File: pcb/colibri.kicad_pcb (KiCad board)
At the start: 2 copper layers, 160 x 95.2 mm, 97 parts

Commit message: starting to build the right side
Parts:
- added REF**: Breakaway_Tabs, kbd:Breakaway_Tabs, F.Cu at (75.0, 134.5)
- added REF**: Breakaway_Tabs, kbd:Breakaway_Tabs, F.Cu at (75.0, 230.2)
- added REF**: Breakaway_Tabs, kbd:Breakaway_Tabs, F.Cu at (24.8, 114.2)
- added REF**: Breakaway_Tabs, kbd:Breakaway_Tabs, F.Cu at (75.0, 38.8)
- added REF**: Breakaway_Tabs, kbd:Breakaway_Tabs, F.Cu at (24.8, 210.0)
- added REF**: Breakaway_Tabs, kbd:Breakaway_Tabs, F.Cu at (24.8, 154.8)
- added REF**: Breakaway_Tabs, kbd:Breakaway_Tabs, F.Cu at (24.8, 59.0)
- added REF**: Breakaway_Tabs, kbd:Breakaway_Tabs, F.Cu at (135.0, 134.5)
- added REF**: Breakaway_Tabs, kbd:Breakaway_Tabs, F.Cu at (185.2, 114.2)
- added REF**: Breakaway_Tabs, kbd:Breakaway_Tabs, F.Cu at (185.2, 59.0)
- added REF**: Breakaway_Tabs, kbd:Breakaway_Tabs, F.Cu at (135.0, 38.8)
- added REF**: Breakaway_Tabs, kbd:Breakaway_Tabs, F.Cu at (185.2, 154.8)
- added REF**: Breakaway_Tabs, kbd:Breakaway_Tabs, F.Cu at (185.2, 210.0)
- added REF**: Breakaway_Tabs, kbd:Breakaway_Tabs, F.Cu at (135.0, 230.2)
- added Ref**: Val**, kbd:M2_HOLE_v3, F.Cu at (51.8, 210.9)
- added Ref**: Val**, kbd:M2_HOLE_v3, F.Cu at (51.8, 153.8)
- added Ref**: Val**, kbd:M2_HOLE_v3, F.Cu at (165.0, 210.9)
- added Ref**: Val**, kbd:M2_HOLE_v3, F.Cu at (158.2, 153.8)
- added pro-micro2: ProMicro, kbd:ProMicro_v4, B.Cu at (172.1, 156.1)
- added rd-1: 1N4148W, kbd:D3_SMD_v2, B.Cu at (166.1, 144.3)
- added rd-10: 1N4148W, kbd:D3_SMD_v2, B.Cu at (89.9, 163.3)
- added rd-11: 1N4148W, kbd:D3_SMD_v2, B.Cu at (70.9, 163.3)
- added rd-12: 1N4148W, kbd:D3_SMD_v2, B.Cu at (51.8, 163.3)
- added rd-13: 1N4148W, kbd:D3_SMD_v2, B.Cu at (170.9, 182.4)
- added rd-14: 1N4148W, kbd:D3_SMD_v2, B.Cu at (128.0, 182.4)
- added rd-15: 1N4148W, kbd:D3_SMD_v2, B.Cu at (109.0, 182.4)
- added rd-16: 1N4148W, kbd:D3_SMD_v2, B.Cu at (89.9, 182.4)
- added rd-17: 1N4148W, kbd:D3_SMD_v2, B.Cu at (70.9, 182.4)
- added rd-18: 1N4148W, kbd:D3_SMD_v2, B.Cu at (51.8, 182.4)
- added rd-19: 1N4148W, kbd:D3_SMD_v2, B.Cu at (180.4, 201.4)
- added rd-2: 1N4148W, kbd:D3_SMD_v2, B.Cu at (128.0, 144.3)
- added rd-20: 1N4148W, kbd:D3_SMD_v2, B.Cu at (128.0, 201.4)
- added rd-21: 1N4148W, kbd:D3_SMD_v2, B.Cu at (109.0, 201.4)
- added rd-22: 1N4148W, kbd:D3_SMD_v2, B.Cu at (89.9, 201.4)
- added rd-23: 1N4148W, kbd:D3_SMD_v2, B.Cu at (70.9, 201.4)
- added rd-24: 1N4148W, kbd:D3_SMD_v2, B.Cu at (51.8, 201.4)
- added rd-25: 1N4148W, kbd:D3_SMD_v2, B.Cu at (104.2, 220.5)
- added rd-26: 1N4148W, kbd:D3_SMD_v2, B.Cu at (80.4, 220.5)
- added rd-27: 1N4148W, kbd:D3_SMD_v2, B.Cu at (56.6, 220.5)
- added rd-3: 1N4148W, kbd:D3_SMD_v2, B.Cu at (109.0, 144.3)
- added rd-4: 1N4148W, kbd:D3_SMD_v2, B.Cu at (89.9, 144.3)
- added rd-5: 1N4148W, kbd:D3_SMD_v2, B.Cu at (70.9, 144.3)
- added rd-6: 1N4148W, kbd:D3_SMD_v2, B.Cu at (51.8, 144.3)
- added rd-7: 1N4148W, kbd:D3_SMD_v2, B.Cu at (156.6, 163.3)
- added rd-8: 1N4148W, kbd:D3_SMD_v2, B.Cu at (128.0, 163.3)
- added rd-9: 1N4148W, kbd:D3_SMD_v2, B.Cu at (109.0, 163.3)
- added rjack-1: MJ-4PP-9, kbd:MJ-4PP-9_1side, B.Cu at (29.9, 134.6)
- added rled-1: YS-SK6812MINI-E, kbd:YS-SK6812MINI-E, B.Cu at (147.1, 148.8)
- added rled-10: YS-SK6812MINI-E, kbd:YS-SK6812MINI-E, B.Cu at (80.4, 167.8)
- added rled-11: YS-SK6812MINI-E, kbd:YS-SK6812MINI-E, B.Cu at (61.4, 167.8)
- added rled-12: YS-SK6812MINI-E, kbd:YS-SK6812MINI-E, B.Cu at (42.3, 167.8)
- added rled-13: YS-SK6812MINI-E, kbd:YS-SK6812MINI-E, B.Cu at (149.5, 186.9)
- added rled-14: YS-SK6812MINI-E, kbd:YS-SK6812MINI-E, B.Cu at (118.5, 186.9)
- added rled-15: YS-SK6812MINI-E, kbd:YS-SK6812MINI-E, B.Cu at (99.5, 186.9)
- added rled-16: YS-SK6812MINI-E, kbd:YS-SK6812MINI-E, B.Cu at (80.4, 186.9)
- added rled-17: YS-SK6812MINI-E, kbd:YS-SK6812MINI-E, B.Cu at (61.4, 186.9)
- added rled-18: YS-SK6812MINI-E, kbd:YS-SK6812MINI-E, B.Cu at (42.3, 186.9)
- added rled-19: YS-SK6812MINI-E, kbd:YS-SK6812MINI-E, B.Cu at (154.2, 205.9)
- added rled-2: YS-SK6812MINI-E, kbd:YS-SK6812MINI-E, B.Cu at (118.5, 148.8)
- added rled-20: YS-SK6812MINI-E, kbd:YS-SK6812MINI-E, B.Cu at (118.5, 205.9)
- added rled-21: YS-SK6812MINI-E, kbd:YS-SK6812MINI-E, B.Cu at (99.5, 205.9)
- added rled-22: YS-SK6812MINI-E, kbd:YS-SK6812MINI-E, B.Cu at (80.4, 205.9)
- added rled-23: YS-SK6812MINI-E, kbd:YS-SK6812MINI-E, B.Cu at (61.4, 205.9)
- added rled-24: YS-SK6812MINI-E, kbd:YS-SK6812MINI-E, B.Cu at (42.3, 205.9)
- added rled-25: YS-SK6812MINI-E, kbd:YS-SK6812MINI-E, B.Cu at (92.3, 225.0)
- added rled-26: YS-SK6812MINI-E, kbd:YS-SK6812MINI-E, B.Cu at (68.5, 225.0)
- added rled-27: YS-SK6812MINI-E, kbd:YS-SK6812MINI-E, B.Cu at (44.7, 225.0)
- added rled-3: YS-SK6812MINI-E, kbd:YS-SK6812MINI-E, B.Cu at (99.8, 148.8)
- added rled-4: YS-SK6812MINI-E, kbd:YS-SK6812MINI-E, B.Cu at (80.4, 148.8)
- added rled-5: YS-SK6812MINI-E, kbd:YS-SK6812MINI-E, B.Cu at (61.4, 148.8)
- added rled-6: YS-SK6812MINI-E, kbd:YS-SK6812MINI-E, B.Cu at (42.3, 148.8)
- added rled-7: YS-SK6812MINI-E, kbd:YS-SK6812MINI-E, B.Cu at (142.3, 167.8)
- added rled-8: YS-SK6812MINI-E, kbd:YS-SK6812MINI-E, B.Cu at (118.5, 167.8)
- added rled-9: YS-SK6812MINI-E, kbd:YS-SK6812MINI-E, B.Cu at (99.5, 167.8)
- added rreset-1: SW_PUSH, kbd:ResetSW_4P, B.Cu at (171.8, 186.1)
- added rsw-1: SW_PUSH, kbd:CherryMX_Hotswap_2u, F.Cu at (147.1, 144.3)
- added rsw-10: SW_PUSH, kbd:CherryMX_Hotswap, F.Cu at (80.4, 163.3)
- added rsw-11: SW_PUSH, kbd:CherryMX_Hotswap, F.Cu at (61.4, 163.3)
- added rsw-12: SW_PUSH, kbd:CherryMX_Hotswap, F.Cu at (42.3, 163.3)
- added rsw-13: SW_PUSH, kbd:CherryMX_Hotswap_2.25u, F.Cu at (149.5, 182.4)
- added rsw-14: SW_PUSH, kbd:CherryMX_Hotswap, F.Cu at (118.5, 182.4)
- added rsw-15: SW_PUSH, kbd:CherryMX_Hotswap, F.Cu at (99.5, 182.4)
- added rsw-16: SW_PUSH, kbd:CherryMX_Hotswap, F.Cu at (80.4, 182.4)
- added rsw-17: SW_PUSH, kbd:CherryMX_Hotswap, F.Cu at (61.4, 182.4)
- added rsw-18: SW_PUSH, kbd:CherryMX_Hotswap, F.Cu at (42.3, 182.4)
- added rsw-19: SW_PUSH, kbd:CherryMX_Hotswap_2.75u, F.Cu at (154.2, 201.4)
- added rsw-2: SW_PUSH, kbd:CherryMX_Hotswap, F.Cu at (118.5, 144.3)
- added rsw-20: SW_PUSH, kbd:CherryMX_Hotswap, F.Cu at (118.5, 201.4)
- added rsw-21: SW_PUSH, kbd:CherryMX_Hotswap, F.Cu at (99.5, 201.4)
- added rsw-22: SW_PUSH, kbd:CherryMX_Hotswap, F.Cu at (80.4, 201.4)
- added rsw-23: SW_PUSH, kbd:CherryMX_Hotswap, F.Cu at (61.4, 201.4)
- added rsw-24: SW_PUSH, kbd:CherryMX_Hotswap, F.Cu at (42.3, 201.4)
- added rsw-25: SW_PUSH, kbd:CherryMX_Hotswap_1.25u, F.Cu at (92.3, 220.5)
- added rsw-26: SW_PUSH, kbd:CherryMX_Hotswap_1.25u, F.Cu at (68.5, 220.5)
- added rsw-27: SW_PUSH, kbd:CherryMX_Hotswap_1.25u, F.Cu at (44.7, 220.5)
- added rsw-3: SW_PUSH, kbd:CherryMX_Hotswap, F.Cu at (99.5, 144.3)
- added rsw-4: SW_PUSH, kbd:CherryMX_Hotswap, F.Cu at (80.4, 144.3)
- added rsw-5: SW_PUSH, kbd:CherryMX_Hotswap, F.Cu at (61.4, 144.3)
- added rsw-6: SW_PUSH, kbd:CherryMX_Hotswap, F.Cu at (42.3, 144.3)
- added rsw-7: SW_PUSH, kbd:CherryMX_Hotswap_1.5u, F.Cu at (142.3, 163.3)
- added rsw-8: SW_PUSH, kbd:CherryMX_Hotswap, F.Cu at (118.5, 163.3)
- added rsw-9: SW_PUSH, kbd:CherryMX_Hotswap, F.Cu at (99.5, 163.3)
- added ru-1: WS2812B, LED_SMD:LED_WS2812B_PLCC4_5.0x5.0mm_P3.2mm, B.Cu at (149.5, 153.8)
- added ru-2: WS2812B, LED_SMD:LED_WS2812B_PLCC4_5.0x5.0mm_P3.2mm, B.Cu at (99.5, 153.8)
- added ru-3: WS2812B, LED_SMD:LED_WS2812B_PLCC4_5.0x5.0mm_P3.2mm, B.Cu at (42.3, 153.8)
- added ru-4: WS2812B, LED_SMD:LED_WS2812B_PLCC4_5.0x5.0mm_P3.2mm, B.Cu at (149.5, 210.9)
- added ru-5: WS2812B, LED_SMD:LED_WS2812B_PLCC4_5.0x5.0mm_P3.2mm, B.Cu at (99.5, 210.9)
- added ru-6: WS2812B, LED_SMD:LED_WS2812B_PLCC4_5.0x5.0mm_P3.2mm, B.Cu at (42.3, 210.9)
- moved Ref** 4.12 mm to (45.0, 115.2)
- moved Ref** 4.12 mm to (51.9, 58.0)
- moved Ref** 4.12 mm to (158.2, 115.2)
- moved Ref** 4.12 mm to (158.2, 58.0)
- moved ld-1 4.12 mm to (80.0, 48.5)
- moved ld-10 4.12 mm to (137.1, 67.6)
- moved ld-11 4.12 mm to (156.2, 67.6)
- moved ld-12 4.12 mm to (175.2, 67.6)
- moved ld-13 4.12 mm to (72.8, 86.6)
- moved ld-14 4.12 mm to (99.0, 86.6)
- moved ld-15 4.12 mm to (118.0, 86.6)
- moved ld-16 4.12 mm to (137.1, 86.6)
- moved ld-17 4.12 mm to (156.2, 86.6)
- moved ld-18 4.12 mm to (175.2, 86.6)
- moved ld-19 4.12 mm to (68.0, 105.7)
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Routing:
- net lVCC: track 853.0 -> 849.0 mm
- net lGND: track 877.6 -> 876.9 mm
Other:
- board size 160 x 95.2 mm -> 169 x 202.2 mm

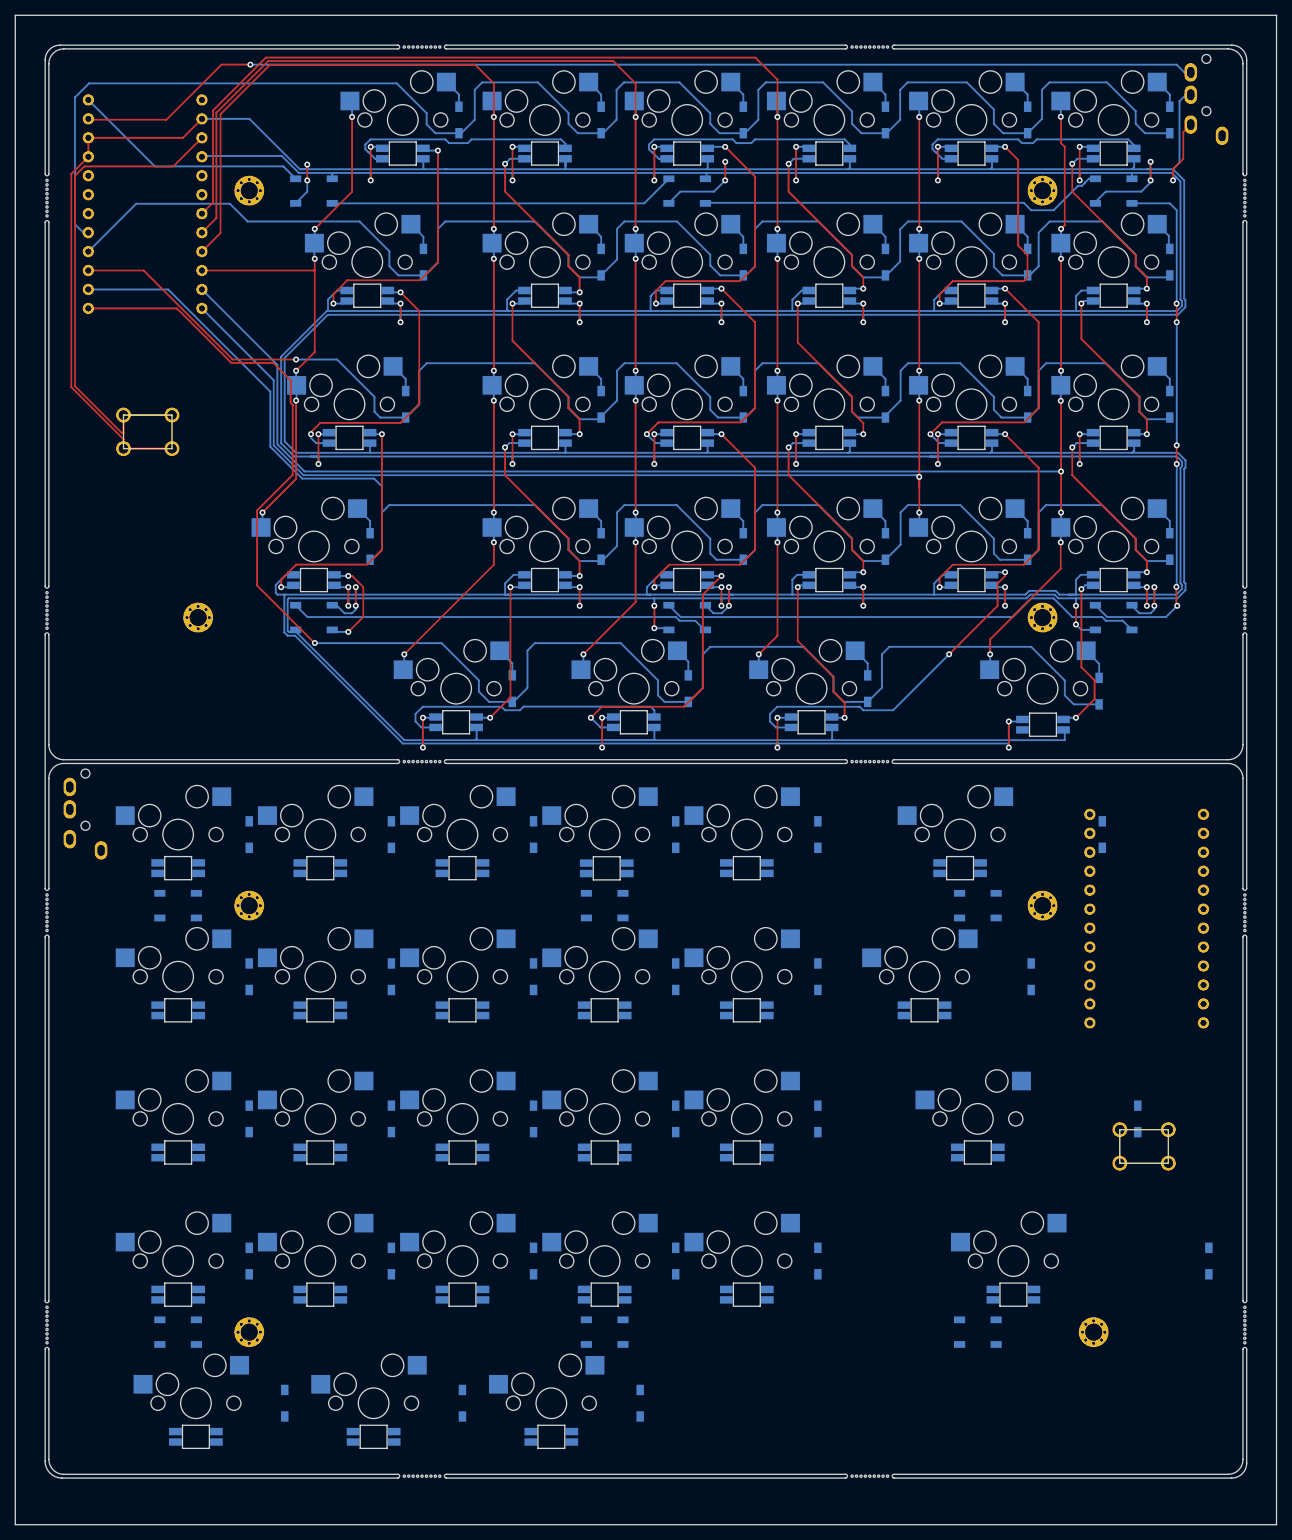
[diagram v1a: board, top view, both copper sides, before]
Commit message: fixed gnd and vcc width for left side pcb
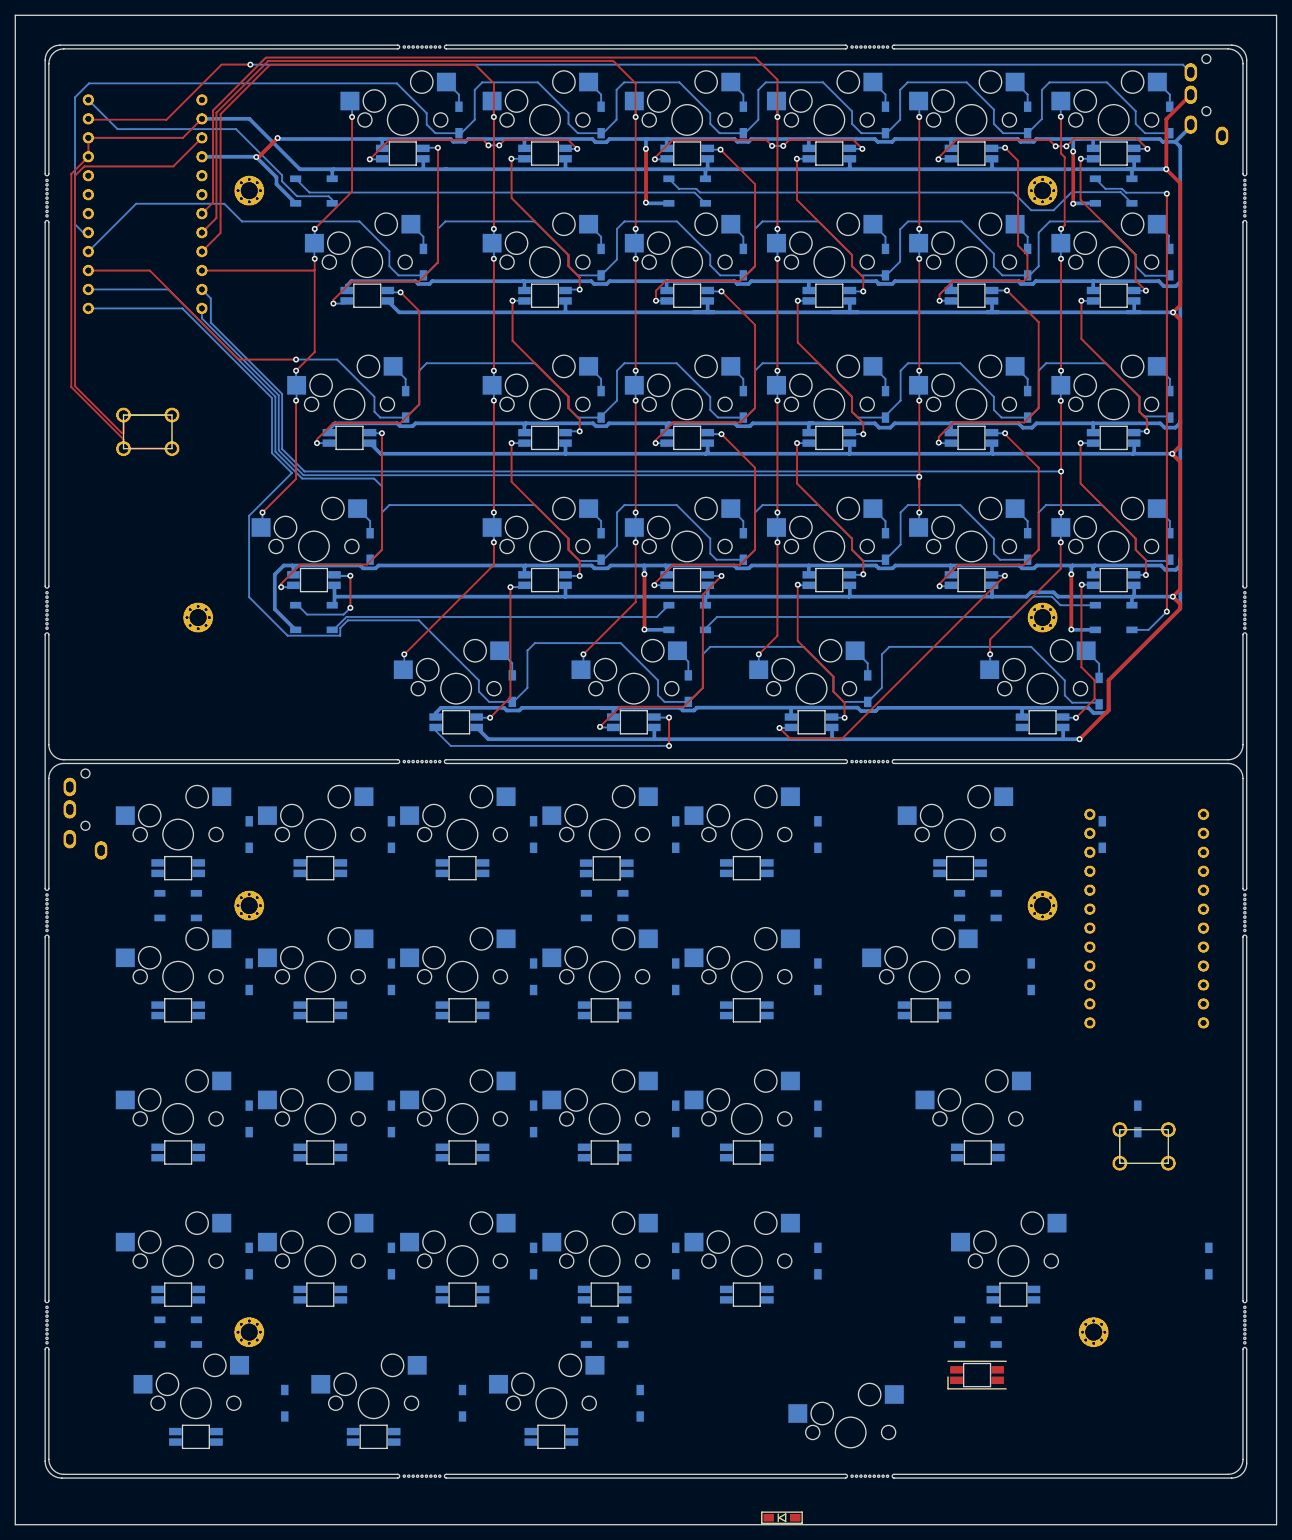
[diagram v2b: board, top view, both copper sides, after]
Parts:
- added rd-28: 1N4148W, kbd:D3_SMD_v2, F.Cu at (123.2, 235.8)
- added rled-28: YS-SK6812MINI-E, kbd:YS-SK6812MINI-E, F.Cu at (149.4, 216.7)
- added rsw-28: SW_PUSH, kbd:CherryMX_Hotswap_1.25u, F.Cu at (132.4, 224.4)
- moved lled-28 0.33 mm to (158.2, 129.2)
- turned lu-1 to 0 degrees
- turned lu-2 to 0 degrees
- turned lu-3 to 0 degrees
- turned lu-4 to 0 degrees
- turned lu-5 to 0 degrees
- turned lu-6 to 0 degrees
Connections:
- net lGND renamed GND1
- net lVCC renamed VCC
- rled-21 pad 4: Net-(rled-20-Pad2) -> Net-(rled-21-Pad4)
- rled-25 pad 2: Net-(rled-25-Pad2) -> Net-(rled-21-Pad4)
- rled-25 pad 4: Net-(rled-22-Pad2) -> Net-(rled-20-Pad2)
- rled-26 pad 2: Net-(rled-23-Pad4) -> Net-(rled-26-Pad2)
- rled-26 pad 4: Net-(rled-25-Pad2) -> Net-(rled-22-Pad2)
- rled-27 pad 2: unconnected-(rled-27-Pad2) -> Net-(rled-23-Pad4)
- rled-27 pad 4: Net-(rled-24-Pad2) -> Net-(rled-26-Pad2)
- rsw-25 pad 1: rcol3 -> rcol2
- rsw-26 pad 1: rcol4 -> rcol3
- rsw-27 pad 1: rcol5 -> rcol4
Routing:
- net GND1: track 876.9 -> 761.5 mm, vias 34 -> 5
- net VCC: track 849.0 -> 765.7 mm, vias 39 -> 10
- net Net-(lu-5-Pad4): track 65.5 -> 54.5 mm
- net Net-(lu-2-Pad2): track 54.4 -> 65.0 mm
- net Net-(lu-4-Pad4): track 56.1 -> 46.3 mm
- net Net-(lu-1-Pad2): track 46.5 -> 56.3 mm
- net lled: track 32.2 -> 39.2 mm
- net Net-(lled-23-Pad4): track 47.4 -> 42.9 mm
- net Net-(lled-19-Pad4): track 14.0 -> 16.9 mm
- net Net-(lled-21-Pad4): track 37.9 -> 35.5 mm
- net Net-(lled-15-Pad2): track 38.6 -> 36.2 mm
- net Net-(lled-5-Pad2): track 32.1 -> 34.0 mm, vias 0 -> 4
- net Net-(lled-13-Pad2): track 37.0 -> 35.3 mm
- net Net-(lled-11-Pad4): track 38.6 -> 36.9 mm
- net lrow4: track 211.2 -> 212.7 mm, vias 1 -> 0
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
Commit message: all components placed on the right position
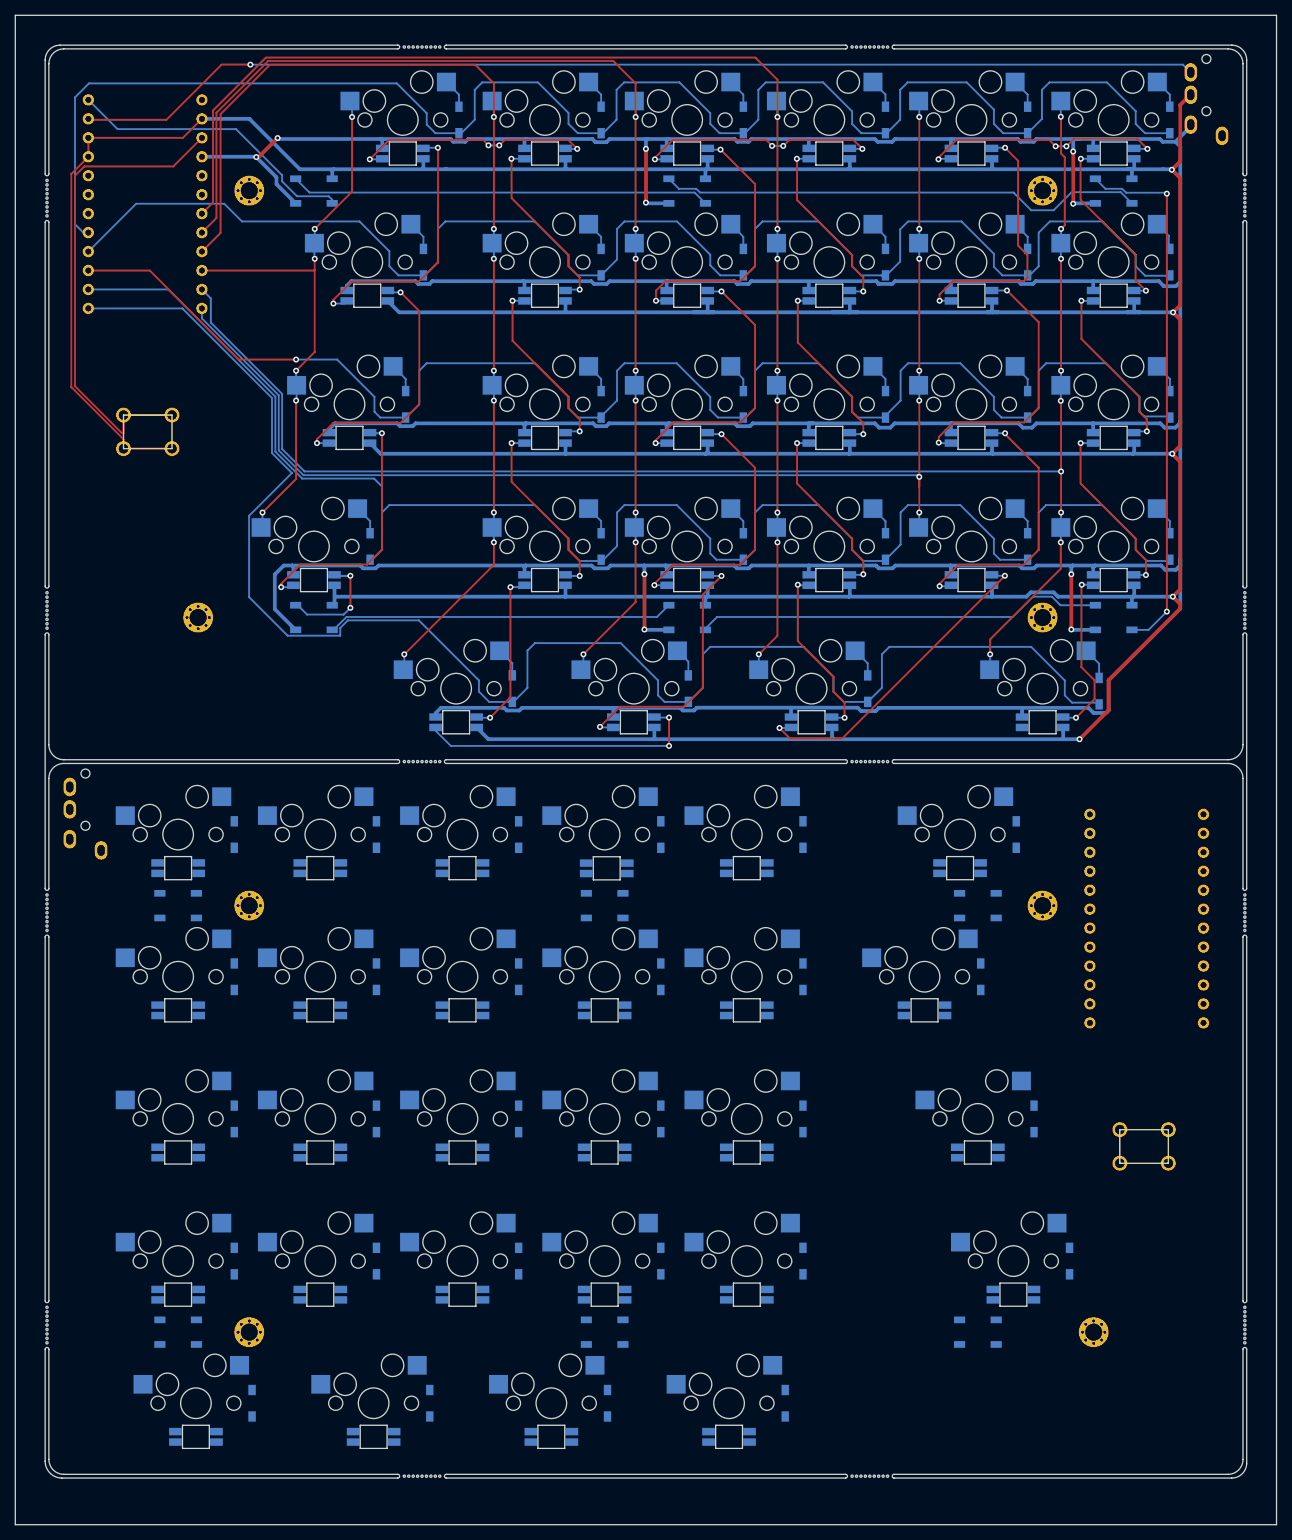
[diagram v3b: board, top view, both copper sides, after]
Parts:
- rd-28, rled-28: moved to B.Cu
- moved rled-28 105.0 mm to (44.7, 225.0), turned to 180 degrees
- moved rsw-28 87.8 mm to (44.7, 220.5)
- moved rd-28 72.6 mm to (52.2, 220.5), turned to 90 degrees
- moved rled-25 23.8 mm to (116.1, 225.0)
- moved rled-26 23.8 mm to (92.3, 225.0)
- moved rled-27 23.8 mm to (68.5, 225.0)
- moved rsw-25 23.8 mm to (116.1, 220.5)
- moved rsw-26 23.8 mm to (92.3, 220.5)
- moved rsw-27 23.8 mm to (68.5, 220.5)
- moved rd-25 19.4 mm to (123.7, 220.5)
- moved rd-26 19.4 mm to (99.9, 220.5)
- moved rd-27 19.4 mm to (76.0, 220.5)
- moved rd-19 18.7 mm to (161.8, 201.4)
- moved rd-13 13.9 mm to (157.0, 182.4)
- moved rd-1 11.5 mm to (154.6, 144.3)
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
